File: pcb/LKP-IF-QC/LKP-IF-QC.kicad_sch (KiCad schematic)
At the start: 9 parts, among them J1 JST SH, J2 JST SH, J3 LKP SWD .1" Extra Long, J4 LKP I/O .1" Extra Long, J5 INT Passthrough, U1 TCA9406DCTR

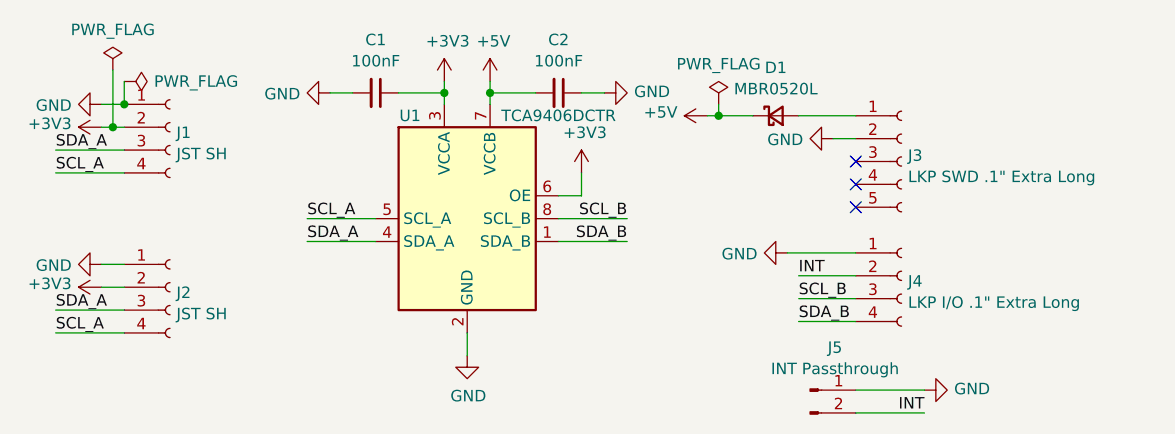
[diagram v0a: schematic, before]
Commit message: Update LKP-IF-Qwiic and bump version to v1.1
- Rename the project from LKP-IF-Qwiic to LKP-IF-QC since Qwiic isn't the only name for this connector.
- Move to KiCad 7.
- Enable teardrops.
- Minor routing tweaks. No schematic change.
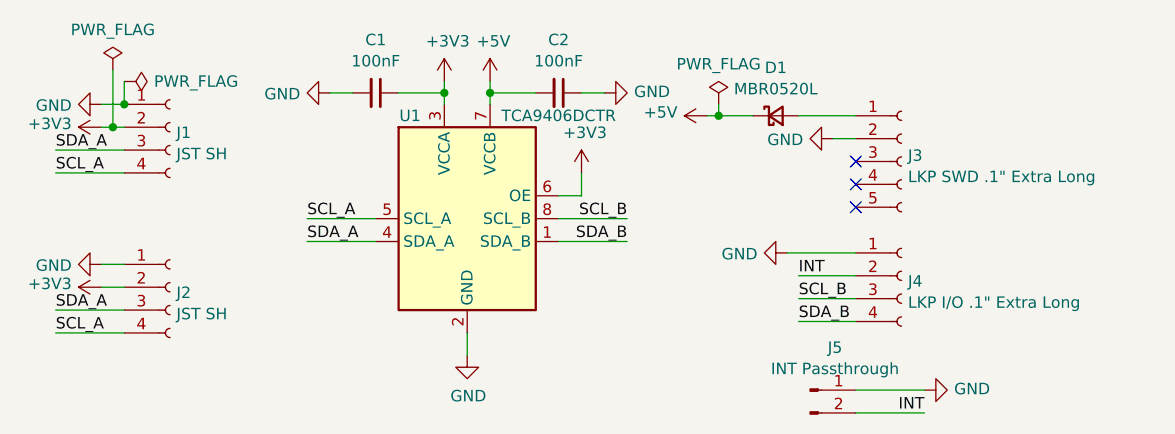
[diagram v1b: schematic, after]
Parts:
- J1, J2, J4: symbol Connector:Conn_01x04_Female -> Connector:Conn_01x04_Socket
- J3: symbol Connector:Conn_01x05_Female -> Connector:Conn_01x05_Socket
- J5: symbol Connector:Conn_01x02_Male -> Connector:Conn_01x02_Pin
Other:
- title: LKP-IF-Qwiic -> LKP-IF-QC
